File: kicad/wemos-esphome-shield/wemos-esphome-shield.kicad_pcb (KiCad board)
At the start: 2 copper layers, 88.7 x 54 mm, 21 parts, among them Q1 2N2219, Q2 2N2219, T1 Transformer_1P_1S, U1 WeMos_D1_mini

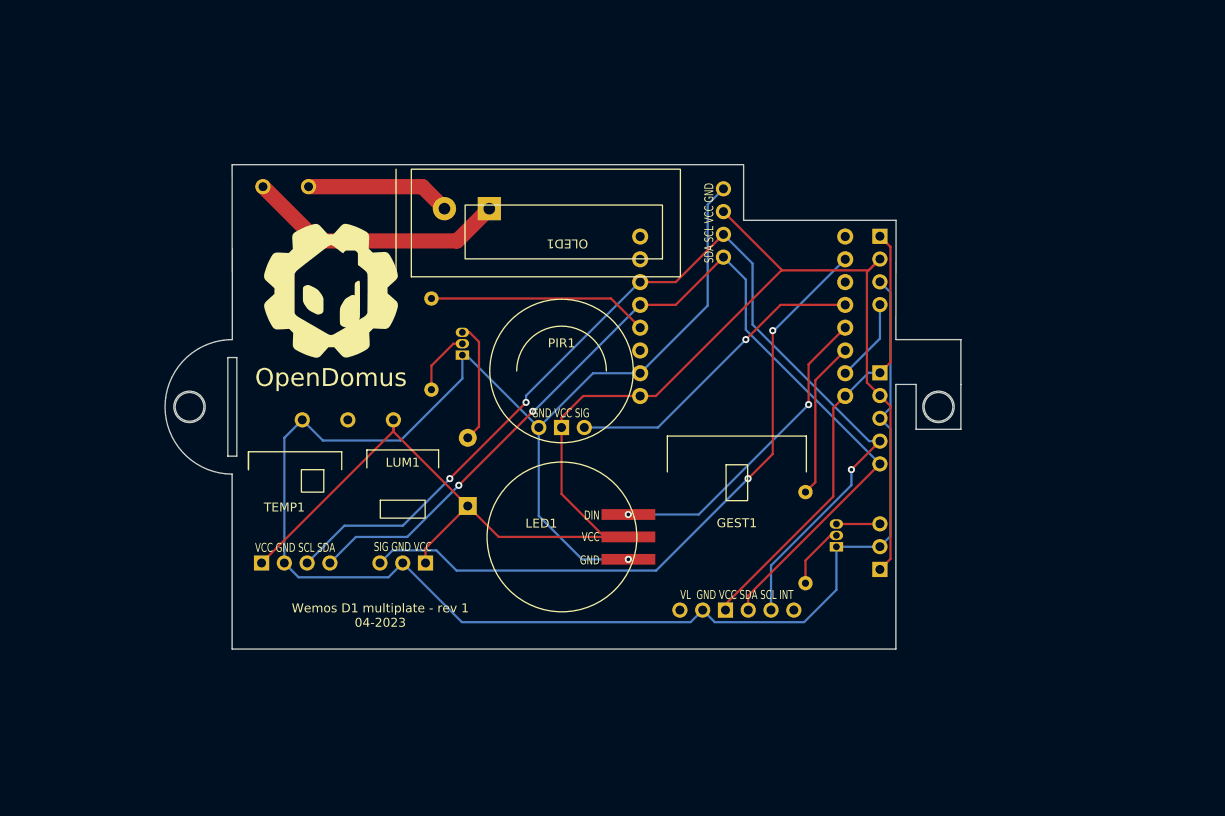
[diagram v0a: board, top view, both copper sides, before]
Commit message: footprint fixes
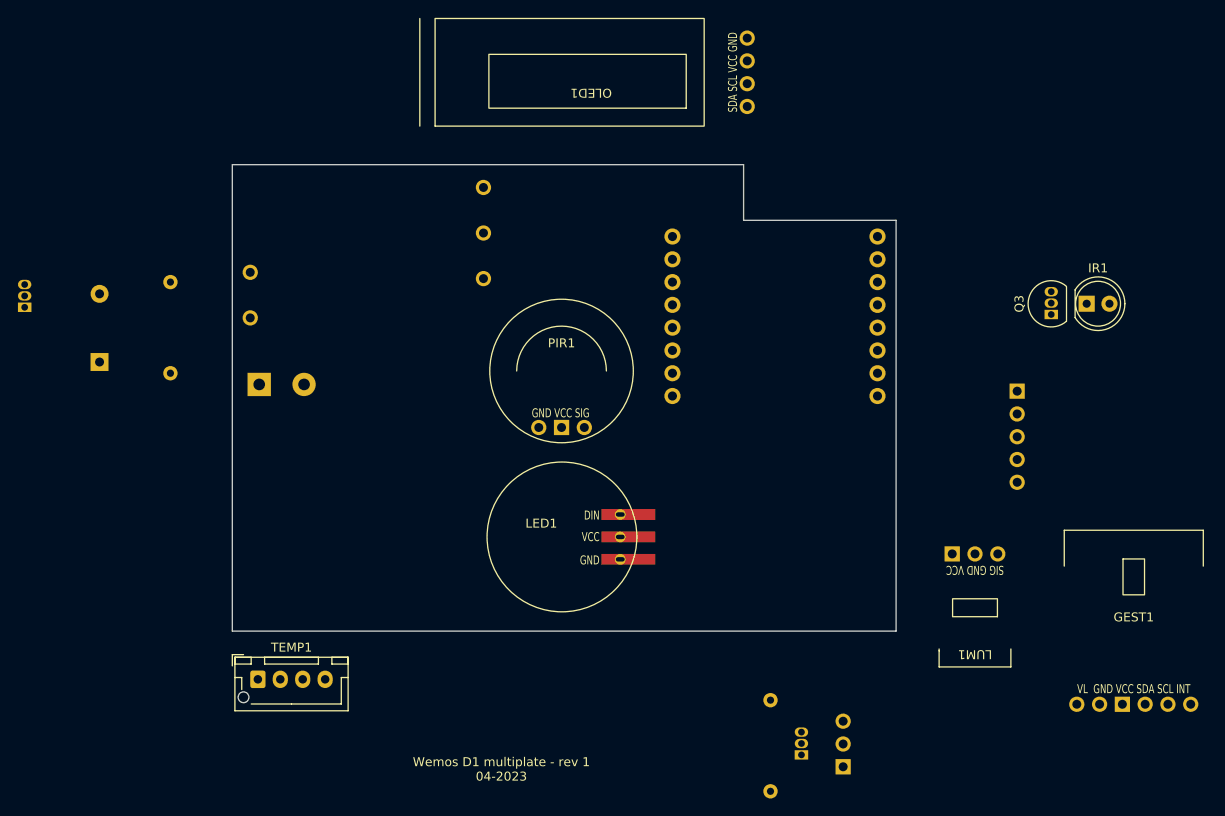
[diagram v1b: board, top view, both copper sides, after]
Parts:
- removed the G*** at (90.0, 78.0)
- removed H1, H2: MountingHole, MountingHole:MountingHole_3.2mm_M3
- removed PIN2: Conn_01x04_Female, Connector_PinHeader_2.54mm:PinHeader_1x04_P2.54mm_Vertical
- added IR1: LED, LED_THT:LED_D5.0mm, F.Cu at (174.2, 79.5)
- added Q3: 2N2219, Package_TO_SOT_THT:TO-92L_Inline, F.Cu at (170.3, 80.7)
- TEMP1: footprint internal:BME280 -> Connector_JST:JST_XH_B4B-XH-AM_1x04_P2.50mm_Vertical
- moved G*** 69.9 mm to (167.3, 56.4)
- moved LUM1 63.8 mm to (161.8, 107.4), turned to 180 degrees
- moved Q1 49.1 mm to (55.9, 79.9)
- moved GEST1 45.5 mm to (179.5, 124.2)
- moved BZ1 44.1 mm to (64.2, 86.0)
- moved POWER1 32.3 mm to (82.0, 88.5), turned to 0 degrees
- moved R1 29.2 mm to (72.1, 77.1)
- moved Q2 23.5 mm to (142.4, 129.8)
- moved R2 23.5 mm to (139.0, 123.7)
- moved RELAY1 22.4 mm to (147.1, 131.1)
- moved OLED1 17.0 mm to (136.4, 53.7)
- moved PIN1 15.4 mm to (166.5, 89.2)
- moved TEMP1 13.3 mm to (81.8, 121.4)
- moved T1 7.07 mm to (94.0, 74.0), turned to 0 degrees
- moved U1 3.60 mm to (139.5, 80.9)
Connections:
- U1 pad 11: unconnected-(U1-Pad11) -> D4
- U1 pad 7: D8 -> unconnected-(U1-Pad7)
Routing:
- net GND: track 222.3 -> 0.00 mm, vias 1 -> 0
- net 5V: track 169.5 -> 0.00 mm
- net SCL: track 116.9 -> 0.00 mm, vias 3 -> 0
- net SDA: track 110.6 -> 0.00 mm, vias 2 -> 0
- net A0: track 75.8 -> 0.00 mm, vias 2 -> 0
- net 3.3V: track 50.5 -> 0.00 mm
- net D6: track 35.4 -> 0.00 mm, vias 2 -> 0
- net D5: track 34.7 -> 0.00 mm, vias 1 -> 0
- net L: track 29.2 -> 0.00 mm
- net D3: track 24.6 -> 0.00 mm
- net D7: track 17.6 -> 0.00 mm
- net N: track 16.2 -> 0.00 mm
- net Net-(BZ1-Pad2): track 13.5 -> 0.00 mm
- net D8: track 9.25 -> 0.00 mm
- net Net-(Q2-Pad2): track 7.14 -> 0.00 mm
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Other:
- board size 88.7 x 54 mm -> 74 x 52 mm
- board text added: "SIG VCC GND"
- board text removed: "3.3 5v GND D8"
- board text removed: "D5 VCC GND"
- board text removed: "RELAY"
- board text removed: "SCL SDA VCC GND"

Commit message: first positioning of footprints
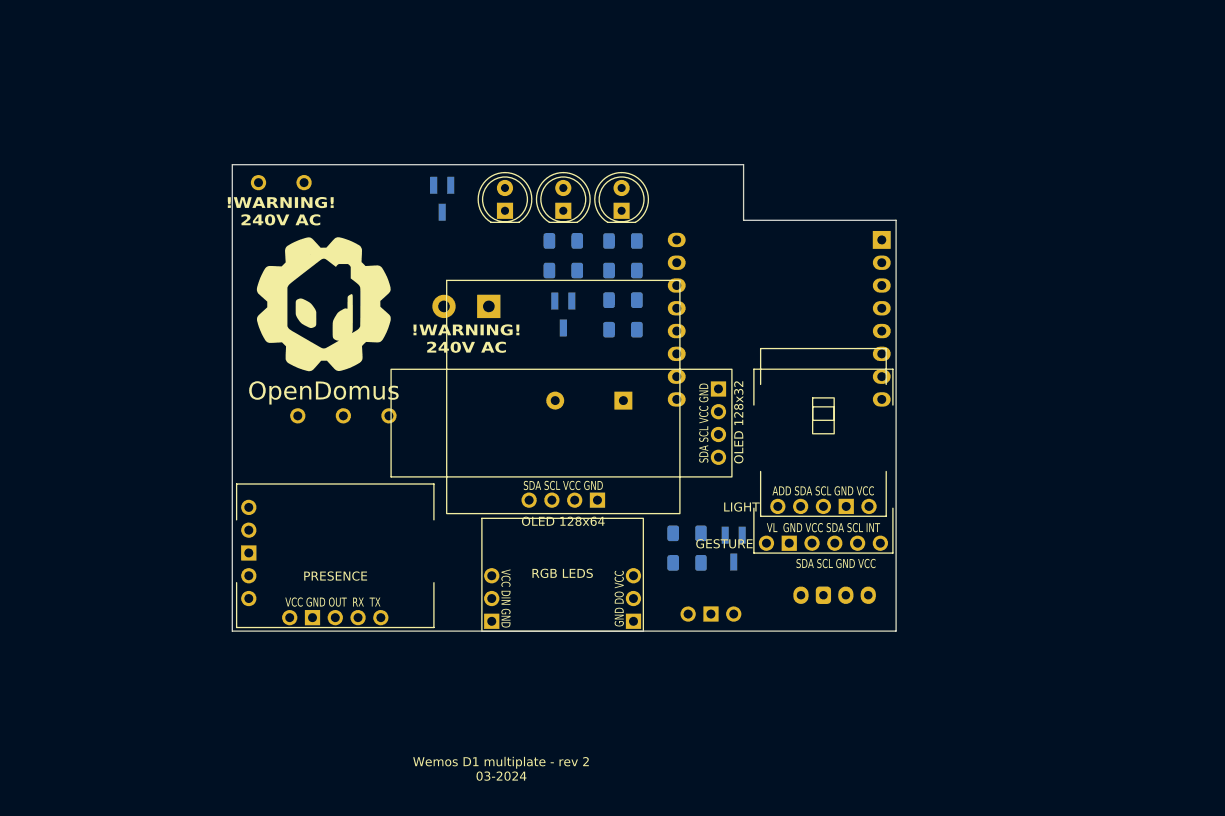
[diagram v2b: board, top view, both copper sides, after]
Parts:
- removed PIN1: Conn_01x05_Female, Connector_PinHeader_2.54mm:PinHeader_1x05_P2.54mm_Vertical
- removed PIR1: Conn_01x03_Female, internal:SR602
- added EXTRA1: PinHeader, Connector_PinHeader_2.54mm:PinHeader_1x05_P2.54mm_Vertical, B.Cu at (80.8, 112.4)
- added IR2: LED, LED_THT:LED_D5.0mm, F.Cu at (115.9, 69.1)
- added IR3: LED, LED_THT:LED_D5.0mm, F.Cu at (109.4, 69.1)
- added MOV1: LD2410C, internal:LD2410C, F.Cu at (90.5, 114.5)
- added OLED2: SSD1306, internal:SSD1306 OLED 128x64, F.Cu at (115.9, 101.4)
- added R3: 100ohm, Resistor_SMD:R_1206_3216Metric_Pad1.30x1.75mm_HandSolder, B.Cu at (122.5, 72.5)
- added R4: 100ohm, Resistor_SMD:R_1206_3216Metric_Pad1.30x1.75mm_HandSolder, B.Cu at (122.5, 75.8)
- added R5: 2kohm, Resistor_SMD:R_1206_3216Metric_Pad1.30x1.75mm_HandSolder, B.Cu at (129.7, 108.4)
- added R6: 2kohm, Resistor_SMD:R_1206_3216Metric_Pad1.30x1.75mm_HandSolder, B.Cu at (115.9, 75.8)
- added R7: 10kohm, Resistor_SMD:R_1206_3216Metric_Pad1.30x1.75mm_HandSolder, B.Cu at (129.7, 105.1)
- added R8: 10kohm, Resistor_SMD:R_1206_3216Metric_Pad1.30x1.75mm_HandSolder, B.Cu at (115.9, 72.5)
- G***: moved to F.Cu
- GEST1: value Conn_01x05_Female -> APDS9960
- LED1: value Conn_01x03_Female -> WS2812B; footprint internal:LED ring -> internal:LED breakout
- LUM1: value Conn_01x03_Female -> BH1750; footprint internal:TEMT6000 -> internal:BH1750
- OLED1: value Conn_01x04_Female -> SSD1306
- Q1, Q2: footprint Package_TO_SOT_THT:TO-92L_Inline -> Package_TO_SOT_SMD:SOT-23_Handsoldering
- Q3: footprint Package_TO_SOT_THT:TO-92L_Inline -> Package_TO_SOT_SMD:SOT-23_Handsoldering; moved to B.Cu
- R1: value R_Small -> 2kohm; footprint Resistor_THT:R_Axial_DIN0207_L6.3mm_D2.5mm_P10.16mm_Horizontal -> Resistor_SMD:R_1206_3216Metric_Pad1.30x1.75mm_HandSolder
- R2: value R_Small -> 10kohm; footprint Resistor_THT:R_Axial_DIN0207_L6.3mm_D2.5mm_P10.16mm_Horizontal -> Resistor_SMD:R_1206_3216Metric_Pad1.30x1.75mm_HandSolder
- RELAY1: value Conn_01x03_Female -> PinHeader
- TEMP1: value Conn_01x04_Female -> SHT30; footprint Connector_JST:JST_XH_B4B-XH-AM_1x04_P2.50mm_Vertical -> Connector_JST:JST_XH_B4B-XH-A_1x04_P2.50mm_Vertical; moved to B.Cu
- U1: footprint wemos-d1-mini:wemos-d1-mini-with-pin-header -> Module:WEMOS_D1_mini_light
- moved G*** 81.4 mm to (89.2, 79.5), turned to 0 degrees
- moved Q3 69.1 mm to (102.4, 67.8), turned to -90 degrees
- moved TEMP1 68.7 mm to (149.9, 112.0), turned to 180 degrees
- moved Q1 60.1 mm to (115.9, 80.7), turned to -90 degrees
- moved BZ1 58.6 mm to (122.6, 90.3), turned to 180 degrees
- moved IR1 52.9 mm to (122.4, 69.1), turned to 90 degrees
- moved R1 50.7 mm to (122.5, 82.4), turned to 180 degrees
- moved R2 47.5 mm to (122.5, 79.1), turned to 0 degrees
- moved OLED1 39.2 mm to (133.2, 92.8)
- moved GEST1 39.0 mm to (144.9, 106.2)
- moved POWER1 27.0 mm to (107.6, 79.8), turned to 180 degrees
- moved Q2 24.2 mm to (134.9, 106.8), turned to -90 degrees
- moved RELAY1 20.9 mm to (134.9, 114.1), turned to 90 degrees
- moved LUM1 17.7 mm to (144.9, 102.1), turned to 0 degrees
- moved U1 14.6 mm to (151.4, 72.4), turned to 180 degrees
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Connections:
- GEST1 pad 3: 3.3V -> 5V
- IR1 pad 1: Net-(IR1-Pad1) -> Net-(IR1-K)
- IR1 pad 2: 5V -> Net-(IR1-A)
- LED1 pad 1: D6 -> 5V
- LED1 pad 2: 5V -> D5
- LUM1 pad 1: A0 -> unconnected-(LUM1-Pin_1-Pad1)
- LUM1 pad 2: GND -> SDA
- LUM1 pad 3: 5V -> SCL
- OLED1 pad 1: SDA -> GND
- OLED1 pad 2: SCL -> 5V
- OLED1 pad 3: 5V -> SCL
- OLED1 pad 4: GND -> SDA
- POWER1 pad 1: L -> N
- POWER1 pad 2: N -> L
- Q1 pad 2: Net-(Q1-Pad2) -> Net-(Q1-B)
- Q2 pad 2: Net-(Q2-Pad2) -> Net-(Q2-B)
- Q2 pad 3: Net-(Q2-Pad3) -> Net-(Q2-C)
- Q3 pad 2: D4 -> Net-(Q3-B)
- Q3 pad 3: Net-(IR1-Pad1) -> Net-(IR3-K)
- R1 pad 2: Net-(Q1-Pad2) -> Net-(Q1-B)
- R2 pad 1: D7 -> Net-(Q1-B)
- R2 pad 2: Net-(Q2-Pad2) -> GND
- RELAY1 pad 1: 5V -> Net-(Q2-C)
- RELAY1 pad 3: Net-(Q2-Pad3) -> 5V
- TEMP1 pad 1: 5V -> SDA
- TEMP1 pad 2: GND -> SCL
- TEMP1 pad 3: SCL -> GND
- TEMP1 pad 4: SDA -> 5V
- U1 pad 11: D4 -> unconnected-(U1-D4-Pad11)
- U1 pad 15: unconnected-(U1-Pad15) -> RX
- U1 pad 16: unconnected-(U1-Pad16) -> TX
- U1 pad 2: A0 -> unconnected-(U1-A0-Pad2)
- U1 pad 7: unconnected-(U1-Pad7) -> D8
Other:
- board text added: "!WARNING! 240V AC"
- board text added: "3.3V 5V GND SCL SDA"
- board text added: "D7 GND 5V"
- board text added: "EXT.RELAY"
- board text added: "EXTRA PINS"
- board text added: "GESTURE"
- board text added: "LIGHT"
- board text added: "OLED 128x32"
- board text added: "OLED 128x64"
- board text added: "PRESENCE"
- board text added: "RGB LEDS"
- board text added: "TEMPERATURE"
- board text added: "WEMOS D1 MINI"
- board text added: "Wemos D1 multiplate - rev 2 03-2024"
- board text removed: "3.3 5v GND SCL SDA"
- board text removed: "SIG GND 5V"
- board text removed: "SIG VCC GND"
- board text removed: "VCC GND SIG"
- board text removed: "Wemos D1 multiplate - rev 1 04-2023"

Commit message: wire tracks
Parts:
- turned R1 to 0 degrees
- turned R3 to 0 degrees
- turned R4 to 0 degrees
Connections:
- OLED1 pad 1: GND -> SDA
- OLED1 pad 2: 5V -> SCL
- OLED1 pad 3: SCL -> 5V
- OLED1 pad 4: SDA -> GND
- OLED2 pad 1: GND -> SDA
- OLED2 pad 2: 5V -> SCL
- OLED2 pad 3: SCL -> 5V
- OLED2 pad 4: SDA -> GND
- U1 pad 7: D8 -> unconnected-(U1-CS/D8-Pad7)
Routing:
- net GND: track 0.00 -> 244.8 mm
- net 5V: track 0.00 -> 219.6 mm, vias 0 -> 1
- net SCL: track 0.00 -> 105.6 mm, vias 0 -> 2
- net SDA: track 0.00 -> 103.7 mm, vias 0 -> 5
- net 3.3V: track 0.00 -> 79.0 mm, vias 0 -> 2
- net D5: track 0.00 -> 59.4 mm, vias 0 -> 2
- net TX: track 0.00 -> 58.4 mm, vias 0 -> 3
- net RX: track 0.00 -> 55.0 mm, vias 0 -> 3
- net D6: track 0.00 -> 39.9 mm, vias 0 -> 1
- net D7: track 0.00 -> 31.6 mm, vias 0 -> 2
- net L: track 0.00 -> 26.4 mm
- net N: track 0.00 -> 26.3 mm
- net Net-(Q3-B): track 0.00 -> 18.2 mm
- net Net-(Q2-B): track 0.00 -> 11.3 mm
- net Net-(IR1-A): track 0.00 -> 9.90 mm
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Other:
- outline, holes or cut-outs redrawn
- board text added: "SDA SCL GND 5V 3.3V"
- board text removed: "3.3V 5V GND SCL SDA"

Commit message: rev2 sent to jlcpcb
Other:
- board text added: "3.3V"
- board text added: "5V"
- board text added: "GND"
- board text added: "RX"
- board text added: "TX"
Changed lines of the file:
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@@
       (outputformat 1)
       (mirror false)
-      (drillshape 1)
+      (drillshape 0)
       (scaleselection 1)
-      (outputdirectory "")
+      (outputdirectory "gerber/")
     )
   )
@@
     (fp_line (start 1.6 0.8) (end 1.6 -0.8)
       (stroke (width 0.1) (type solid)) (layer "B.Fab"))
-    (pad "1" smd roundrect (at -1.55 0) (size 1.3 1.75) (layers "B.Cu" "B.Paste" "B.Mask") (roundrect_rratio 0.192308)
+    (pad "1" smd roundrect (at -1.55 0) (size 1.3 1.75) (layers "B.Cu" "B.Paste" "B.Mask") (roundrect_rratio 0.1923076923)
       (net 1 "5V") (pintype "passive"))
-    (pad "2" smd roundrect (at 1.55 0) (size 1.3 1.75) (layers "B.Cu" "B.Paste" "B.Mask") (roundrect_rratio 0.192308)
+    (pad "2" smd roundrect (at 1.55 0) (size 1.3 1.75) (layers "B.Cu" "B.Paste" "B.Mask") (roundrect_rratio 0.1923076923)
       (net 16 "Net-(IR1-A)") (pintype "passive"))
     (model "${KICAD6_3DMODEL_DIR}/Resistor_SMD.3dshapes/R_1206_3216Metric.wrl"
@@
     (fp_line (start 1.6 0.8) (end 1.6 -0.8)
       (stroke (width 0.1) (type solid)) (layer "B.Fab"))
-    (pad "1" smd roundrect (at -1.55 0) (size 1.3 1.75) (layers "B.Cu" "B.Paste" "B.Mask") (roundrect_rratio 0.192308)
+    (pad "1" smd roundrect (at -1.55 0) (size 1.3 1.75) (layers "B.Cu" "B.Paste" "B.Mask") (roundrect_rratio 0.1923076923)
       (net 9 "D3") (pintype "passive"))
-    (pad "2" smd roundrect (at 1.55 0) (size 1.3 1.75) (layers "B.Cu" "B.Paste" "B.Mask") (roundrect_rratio 0.192308)
+    (pad "2" smd roundrect (at 1.55 0) (size 1.3 1.75) (layers "B.Cu" "B.Paste" "B.Mask") (roundrect_rratio 0.1923076923)
       (net 24 "Net-(Q1-B)") (pintype "passive"))
     (model "${KICAD6_3DMODEL_DIR}/Resistor_SMD.3dshapes/R_1206_3216Metric.wrl"
@@
     (fp_line (start 1.6 0.8) (end 1.6 -0.8)
       (stroke (width 0.1) (type solid)) (layer "B.Fab"))
-    (pad "1" smd roundrect (at -1.55 0) (size 1.3 1.75) (layers "B.Cu" "B.Paste" "B.Mask") (roundrect_rratio 0.192308)
+    (pad "1" smd roundrect (at -1.55 0) (size 1.3 1.75) (layers "B.Cu" "B.Paste" "B.Mask") (roundrect_rratio 0.1923076923)
       (net 27 "Net-(Q3-B)") (pintype "passive"))
-    (pad "2" smd roundrect (at 1.55 0) (size 1.3 1.75) (layers "B.Cu" "B.Paste" "B.Mask") (roundrect_rratio 0.192308)
+    (pad "2" smd roundrect (at 1.55 0) (size 1.3 1.75) (layers "B.Cu" "B.Paste" "B.Mask") (roundrect_rratio 0.1923076923)
       (net 6 "GND") (pintype "passive"))
     (model "${KICAD6_3DMODEL_DIR}/Resistor_SMD.3dshapes/R_1206_3216Metric.wrl"
@@
     (fp_line (start 1.6 0.8) (end 1.6 -0.8)
       (stroke (width 0.1) (type solid)) (layer "B.Fab"))
-    (pad "1" smd roundrect (at -1.55 0) (size 1.3 1.75) (layers "B.Cu" "B.Paste" "B.Mask") (roundrect_rratio 0.192308)
+    (pad "1" smd roundrect (at -1.55 0) (size 1.3 1.75) (layers "B.Cu" "B.Paste" "B.Mask") (roundrect_rratio 0.1923076923)
       (net 24 "Net-(Q1-B)") (pintype "passive"))
-    (pad "2" smd roundrect (at 1.55 0) (size 1.3 1.75) (layers "B.Cu" "B.Paste" "B.Mask") (roundrect_rratio 0.192308)
+    (pad "2" smd roundrect (at 1.55 0) (size 1.3 1.75) (layers "B.Cu" "B.Paste" "B.Mask") (roundrect_rratio 0.1923076923)
       (net 6 "GND") (pintype "passive"))
     (model "${KICAD6_3DMODEL_DIR}/Resistor_SMD.3dshapes/R_1206_3216Metric.wrl"
@@
     (fp_line (start 1.6 0.8) (end 1.6 -0.8)
       (stroke (width 0.1) (type solid)) (layer "B.Fab"))
-    (pad "1" smd roundrect (at -1.55 0) (size 1.3 1.75) (layers "B.Cu" "B.Paste" "B.Mask") (roundrect_rratio 0.192308)
+    (pad "1" smd roundrect (at -1.55 0) (size 1.3 1.75) (layers "B.Cu" "B.Paste" "B.Mask") (roundrect_rratio 0.1923076923)
       (net 3 "D6") (pintype "passive"))
-    (pad "2" smd roundrect (at 1.55 0) (size 1.3 1.75) (layers "B.Cu" "B.Paste" "B.Mask") (roundrect_rratio 0.192308)
+    (pad "2" smd roundrect (at 1.55 0) (size 1.3 1.75) (layers "B.Cu" "B.Paste" "B.Mask") (roundrect_rratio 0.1923076923)
       (net 27 "Net-(Q3-B)") (pintype "passive"))
     (model "${KICAD6_3DMODEL_DIR}/Resistor_SMD.3dshapes/R_1206_3216Metric.wrl"
@@
     (fp_line (start 1.6 0.8) (end 1.6 -0.8)
       (stroke (width 0.1) (type solid)) (layer "B.Fab"))
-    (pad "1" smd roundrect (at -1.55 0 180) (size 1.3 1.75) (layers "B.Cu" "B.Paste" "B.Mask") (roundrect_rratio 0.192308)
+    (pad "1" smd roundrect (at -1.55 0 180) (size 1.3 1.75) (layers "B.Cu" "B.Paste" "B.Mask") (roundrect_rratio 0.1923076923)
       (net 12 "D7") (pintype "passive"))
-    (pad "2" smd roundrect (at 1.55 0 180) (size 1.3 1.75) (layers "B.Cu" "B.Paste" "B.Mask") (roundrect_rratio 0.192308)
+    (pad "2" smd roundrect (at 1.55 0 180) (size 1.3 1.75) (layers "B.Cu" "B.Paste" "B.Mask") (roundrect_rratio 0.1923076923)
       (net 25 "Net-(Q2-B)") (pintype "passive"))
     (model "${KICAD6_3DMODEL_DIR}/Resistor_SMD.3dshapes/R_1206_3216Metric.wrl"
@@
     (fp_line (start 1.6 0.8) (end 1.6 -0.8)
       (stroke (width 0.1) (type solid)) (layer "B.Fab"))
-    (pad "1" smd roundrect (at -1.55 0 180) (size 1.3 1.75) (layers "B.Cu" "B.Paste" "B.Mask") (roundrect_rratio 0.192308)
+    (pad "1" smd roundrect (at -1.55 0 180) (size 1.3 1.75) (layers "B.Cu" "B.Paste" "B.Mask") (roundrect_rratio 0.1923076923)
       (net 25 "Net-(Q2-B)") (pintype "passive"))
-    (pad "2" smd roundrect (at 1.55 0 180) (size 1.3 1.75) (layers "B.Cu" "B.Paste" "B.Mask") (roundrect_rratio 0.192308)
+    (pad "2" smd roundrect (at 1.55 0 180) (size 1.3 1.75) (layers "B.Cu" "B.Paste" "B.Mask") (roundrect_rratio 0.1923076923)
       (net 6 "GND") (pintype "passive"))
     (model "${KICAD6_3DMODEL_DIR}/Resistor_SMD.3dshapes/R_1206_3216Metric.wrl"
@@
     (fp_line (start 1.6 0.8) (end 1.6 -0.8)
       (stroke (width 0.1) (type solid)) (layer "B.Fab"))
-    (pad "1" smd roundrect (at -1.55 0) (size 1.3 1.75) (layers "B.Cu" "B.Paste" "B.Mask") (roundrect_rratio 0.192308)
+    (pad "1" smd roundrect (at -1.55 0) (size 1.3 1.75) (layers "B.Cu" "B.Paste" "B.Mask") (roundrect_rratio 0.1923076923)
       (net 1 "5V") (pintype "passive"))
-    (pad "2" smd roundrect (at 1.55 0) (size 1.3 1.75) (layers "B.Cu" "B.Paste" "B.Mask") (roundrect_rratio 0.192308)
+    (pad "2" smd roundrect (at 1.55 0) (size 1.3 1.75) (layers "B.Cu" "B.Paste" "B.Mask") (roundrect_rratio 0.1923076923)
       (net 16 "Net-(IR1-A)") (pintype "passive"))
     (model "${KICAD6_3DMODEL_DIR}/Resistor_SMD.3dshapes/R_1206_3216Metric.wrl"
@@
     (effects (font (size 1 1) (thickness 0.15)) (justify mirror))
   )
+  (gr_text "GND" (at 129.7 87.6) (layer "B.SilkS")
+    (effects (font (size 1 1) (thickness 0.15)) (justify right mirror))
+  )
   (gr_text "TEMPERATURE" (at 146.1 108.6) (layer "B.SilkS")
     (effects (font (size 1 1) (thickness 0.15)) (justify mirror))
   )
+  (gr_text "RX" (at 129.8 75) (layer "B.SilkS")
+    (effects (font (size 1 1) (thickness 0.15)) (justify right mirror))
+  )
   (gr_text "EXTRA PINS" (at 84.2 107.3 -90) (layer "B.SilkS")
     (effects (font (size 1 1) (thickness 0.15)) (justify mirror))
   )
+  (gr_text "TX" (at 129.8 72.4) (layer "B.SilkS")
+    (effects (font (size 1 1) (thickness 0.15)) (justify right mirror))
+  )
+  (gr_text "3.3V" (at 150.3 90.2) (layer "B.SilkS")
+    (effects (font (size 1 1) (thickness 0.15)) (justify left mirror))
+  )
+  (gr_text "5V" (at 129.8 90.2) (layer "B.SilkS")
+    (effects (font (size 1 1) (thickness 0.15)) (justify right mirror))
+  )
   (gr_text "Wemos D1 multiplate - rev 2\n03-2024" (at 93.6 97.2) (layer "B.SilkS")
